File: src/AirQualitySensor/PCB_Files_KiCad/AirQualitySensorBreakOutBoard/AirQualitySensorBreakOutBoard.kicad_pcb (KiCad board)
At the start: 2 copper layers, 113.8 x 36 mm, 23 parts, among them J1 Conn_01x02_Male, J2 Conn_01x02_Male, J3 Conn_01x02_Male, J4 Conn_01x07_Male, Q1 IRLB8721PBF, U1 PMS5003, U2 PMS5003, U3 SPS30, U4 SHT31, U6 lilygo-ttgo-t-sim7000g-esp32-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

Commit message: Merged AQS
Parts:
- moved J2 0.95 mm to (93.7, 18.0)
- moved J3 0.85 mm to (93.7, 26.9)
- moved J1 0.50 mm to (93.7, 35.7)
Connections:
- U6 pad 12: unconnected-(U6-Pad12) -> VDD_EN
- U6 pad 13: VDD_EN -> unconnected-(U6-Pad13)
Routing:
- net VDD_EN: track 34.6 -> 31.9 mm
- net Solar_IN: track 41.5 -> 43.6 mm
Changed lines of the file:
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@@
   (net 7 "unconnected-(U6-Pad03)")
   (net 8 "unconnected-(U6-Pad04)")
-  (net 9 "unconnected-(U6-Pad12)")
+  (net 9 "unconnected-(U6-Pad13)")
   (net 10 "unconnected-(U6-Pad14)")
   (net 11 "unconnected-(U6-Pad15)")
@@
   (net 38 "VDD_EN")
   (footprint "Connector_JST:JST_XH_B2B-XH-AM_1x02_P2.50mm_Vertical" (layer "F.Cu")
-    (at 93.725 18.95 -90)
+    (at 93.7 18 -90)
     (descr "JST XH series connector, B2B-XH-AM, with boss (http://www.jst-mfg.com/product/pdf/eng/eXH.pdf), generated with kicad-footprint-generator")
     (tags "connector JST XH vertical boss")
@@
       (net 34 "SPI_SS") (pinfunction "SPI__SS") (pintype "input"))
     (pad "12" thru_hole circle (at -14.12 -4.6 90) (size 2 2) (drill 1.02) (layers *.Cu *.Mask)
-      (net 9 "unconnected-(U6-Pad12)") (pinfunction "12") (pintype "input"))
+      (net 38 "VDD_EN") (pinfunction "12") (pintype "input"))
     (pad "13" thru_hole circle (at -14.12 -7.14 90) (size 2 2) (drill 1.02) (layers *.Cu *.Mask)
-      (net 38 "VDD_EN") (pinfunction "13") (pintype "input"))
+      (net 9 "unconnected-(U6-Pad13)") (pinfunction "13") (pintype "input"))
     (pad "14" thru_hole circle (at -14.12 -9.68 90) (size 2 2) (drill 1.02) (layers *.Cu *.Mask)
       (net 10 "unconnected-(U6-Pad14)") (pinfunction "14") (pintype "input"))
@@
   )
   (footprint "Connector_JST:JST_XH_B2B-XH-AM_1x02_P2.50mm_Vertical" (layer "F.Cu")
-    (at 93.7 36.2 -90)
+    (at 93.7 35.7 -90)
     (descr "JST XH series connector, B2B-XH-AM, with boss (http://www.jst-mfg.com/product/pdf/eng/eXH.pdf), generated with kicad-footprint-generator")
     (tags "connector JST XH vertical boss")
@@
   )
   (footprint "Connector_JST:JST_XH_B2B-XH-AM_1x02_P2.50mm_Vertical" (layer "F.Cu")
-    (at 93.7 27.7 -90)
+    (at 93.7 26.85 -90)
     (descr "JST XH series connector, B2B-XH-AM, with boss (http://www.jst-mfg.com/product/pdf/eng/eXH.pdf), generated with kicad-footprint-generator")
     (tags "connector JST XH vertical boss")
@@
   (segment (start 57.357621 27.882379) (end 55.04 30.2) (width 1) (layer "F.Cu") (net 2))
   (segment (start 25.494649 47.243002) (end 27.537651 45.2) (width 1) (layer "F.Cu") (net 3))
+  (segment (start 93.65 29.4) (end 89.3 29.4) (width 1) (layer "F.Cu") (net 3))
   (segment (start 73.5 14.5) (end 74.9 15.9) (width 1) (layer "F.Cu") (net 3))
   (segment (start 69.4 38.4) (end 62.8 38.4) (width 1) (layer "F.Cu") (net 3))
   (segment (start 69.5 43.7) (end 70.2 43) (width 1) (layer "F.Cu") (net 3))
   (segment (start 44.9 43.7) (end 46.8 43.7) (width 1) (layer "F.Cu") (net 3))
-  (segment (start 93.7 38.7) (end 89.2 38.7) (width 1) (layer "F.Cu") (net 3))
+  (segment (start 93.7 38.35) (end 93.7 38.2) (width 1) (layer "F.Cu") (net 3))
   (segment (start 89.2 35.7) (end 89.2 29.7) (width 1) (layer "F.Cu") (net 3))
+  (segment (start 89.2 29.7) (end 89.2 20) (width 1) (layer "F.Cu") (net 3))
   (segment (start 89.2 38.7) (end 89.2 35.7) (width 1) (layer "F.Cu") (net 3))
-  (segment (start 93.7 30.2) (end 89.7 30.2) (width 1) (layer "F.Cu") (net 3))
   (segment (start 89.2 45.125) (end 89.2 38.7) (width 1) (layer "F.Cu") (net 3))
   (segment (start 46.8 43.7) (end 69.5 43.7) (width 1) (layer "F.Cu") (net 3))
+  (segment (start 89.8 20.4) (end 93.6 20.4) (width 1) (layer "F.Cu") (net 3))
   (segment (start 89.5 45.3) (end 80.2 45.3) (width 1) (layer "F.Cu") (net 3))
   (segment (start 27.537651 45.2) (end 43.4 45.2) (width 1) (layer "F.Cu") (net 3))
-  (segment (start 89.2 21.7) (end 89.45 21.45) (width 1) (layer "F.Cu") (net 3))
+  (segment (start 93.7 29.35) (end 93.65 29.4) (width 1) (layer "F.Cu") (net 3))
   (segment (start 46.617621 43.517621) (end 46.8 43.7) (width 1) (layer "F.Cu") (net 3))
   (segment (start 91.65738 45.3) (end 89.375 45.3) (width 1) (layer "F.Cu") (net 3))
@@
   (segment (start 58.394649 14.605351) (end 58.5 14.5) (width 1) (layer "F.Cu") (net 3))
   (segment (start 70.2 39.2) (end 69.4 38.4) (width 1) (layer "F.Cu") (net 3))
-  (segment (start 89.45 21.45) (end 89.95 21.45) (width 1) (layer "F.Cu") (net 3))
-  (segment (start 89.2 29.7) (end 89.2 21.7) (width 1) (layer "F.Cu") (net 3))
+  (segment (start 93.6 20.4) (end 93.7 20.5) (width 1) (layer "F.Cu") (net 3))
   (segment (start 66.8 35) (end 62 30.2) (width 1) (layer "F.Cu") (net 3))
-  (segment (start 89.95 21.45) (end 89.175 21.45) (width 1) (layer "F.Cu") (net 3))
   (segment (start 91.85738 45.2) (end 91.75738 45.3) (width 1) (layer "F.Cu") (net 3))
   (segment (start 70.2 43) (end 70.2 39.2) (width 1) (layer "F.Cu") (net 3))
   (segment (start 80.2 45.3) (end 69.9 35) (width 1) (layer "F.Cu") (net 3))
   (segment (start 69.9 35) (end 66.8 35) (width 1) (layer "F.Cu") (net 3))
-  (segment (start 89.7 30.2) (end 89.2 29.7) (width 1) (layer "F.Cu") (net 3))
   (segment (start 89.175 21.2) (end 89.175 15.9) (width 1) (layer "F.Cu") (net 3))
   (segment (start 58.394649 16.653002) (end 58.394649 14.605351) (width 1) (layer "F.Cu") (net 3))
-  (segment (start 93.792621 21.517621) (end 93.725 21.45) (width 1) (layer "F.Cu") (net 3))
   (segment (start 57.58 33.18) (end 57.58 30.2) (width 1) (layer "F.Cu") (net 3))
+  (segment (start 93.7 38.2) (end 89.3 38.2) (width 1) (layer "F.Cu") (net 3))
   (segment (start 74.9 15.9) (end 89.1 15.9) (width 1) (layer "F.Cu") (net 3))
   (segment (start 58.5 14.5) (end 73.5 14.5) (width 1) (layer "F.Cu") (net 3))
   (segment (start 91.75738 45.3) (end 91.65738 45.3) (width 1) (layer "F.Cu") (net 3))
-  (segment (start 89.95 21.45) (end 93.725 21.45) (width 1) (layer "F.Cu") (net 3))
   (segment (start 43.4 45.2) (end 44.9 43.7) (width 1) (layer "F.Cu") (net 3))
   (segment (start 30.454649 16.653002) (end 30.454649 14.5) (width 1) (layer "B.Cu") (net 3))
@@
   (segment (start 21.735 32.865) (end 19.5 35.1) (width 1) (layer "B.Cu") (net 32))
   (segment (start 22.894649 45.694649) (end 22.894649 47.263002) (width 1) (layer "B.Cu") (net 32))
-  (segment (start 97.2 28.7) (end 97.2 19.7) (width 1) (layer "F.Cu") (net 33))
-  (segment (start 97.2 27.7) (end 93.7 27.7) (width 1) (layer "F.Cu") (net 33))
+  (segment (start 97.1 26.9) (end 93.75 26.9) (width 1) (layer "F.Cu") (net 33))
+  (segment (start 97.1 35.7) (end 93.7 35.7) (width 1) (layer "F.Cu") (net 33))
+  (segment (start 97.2 18) (end 93.7 18) (width 1) (layer "F.Cu") (net 33))
+  (segment (start 97.2 35.8) (end 97.1 35.7) (width 1) (layer "F.Cu") (net 33))
+  (segment (start 97.2 28.7) (end 97.2 26.8) (width 1) (layer "F.Cu") (net 33))
   (segment (start 97.2 36.2) (end 97.2 28.7) (width 1) (layer "F.Cu") (net 33))
   (segment (start 97.2 37.7) (end 97.2 36.2) (width 1) (layer "F.Cu") (net 33))
   (segment (start 97.2 38.7) (end 97.2 37.7) (width 1) (layer "F.Cu") (net 33))
   (segment (start 97.075 45.3) (end 97.2 45.175) (width 1) (layer "F.Cu") (net 33))
-  (segment (start 96.45 18.95) (end 93.725 18.95) (width 1) (layer "F.Cu") (net 33))
-  (segment (start 97.2 36.2) (end 93.7 36.2) (width 1) (layer "F.Cu") (net 33))
-  (segment (start 97.2 19.7) (end 96.45 18.95) (width 1) (layer "F.Cu") (net 33))
-  (segment (start 97.2 28.7) (end 97.2 27.7) (width 1) (layer "F.Cu") (net 33))
+  (segment (start 97.2 28.7) (end 97.2 18) (width 1) (layer "F.Cu") (net 33))
   (segment (start 97.2 45.175) (end 97.2 37.7) (width 1) (layer "F.Cu") (net 33))
-  (segment (start 93.792621 19.017621) (end 93.725 18.95) (width 1) (layer "F.Cu") (net 33))
+  (segment (start 93.75 26.9) (end 93.7 26.85) (width 1) (layer "F.Cu") (net 33))
   (segment (start 94.15738 45.3) (end 97.075 45.3) (width 1) (layer "F.Cu") (net 33))
   (segment (start 45.694649 17.694649) (end 47.48 19.48) (width 1) (layer "F.Cu") (net 34))
@@
   (segment (start 39.86 20.5) (end 38.085 18.725) (width 1) (layer "F.Cu") (net 37))
   (segment (start 38.085 18.725) (end 38.085 16.663353) (width 1) (layer "F.Cu") (net 37))
-  (segment (start 62.5 33.51) (end 62.5 33.6) (width 1) (layer "F.Cu") (net 38))
+  (segment (start 71.6 43.8) (end 70.174649 45.225351) (width 1) (layer "F.Cu") (net 38))
+  (segment (start 62.5 33.6) (end 65.6 36.7) (width 1) (layer "F.Cu") (net 38))
   (segment (start 71.6 38.8) (end 71.6 43.8) (width 1) (layer "F.Cu") (net 38))
-  (segment (start 69.5 36.7) (end 71.6 38.8) (width 1) (layer "F.Cu") (net 38))
-  (segment (start 70.174649 45.225351) (end 55.974649 45.225351) (width 1) (layer "F.Cu") (net 38))
   (segment (start 65.6 36.7) (end 69.5 36.7) (width 1) (layer "F.Cu") (net 38))
-  (segment (start 55.974649 45.225351) (end 55.974649 47.243002) (width 1) (layer "F.Cu") (net 38))
-  (segment (start 62.5 33.6) (end 65.6 36.7) (width 1) (layer "F.Cu") (net 38))
-  (segment (start 71.6 43.8) (end 70.174649 45.225351) (width 1) (layer "F.Cu") (net 38))
+  (segment (start 62.5 33.51) (end 62.5 33.6) (width 1) (layer "F.Cu") (net 38))
+  (segment (start 69.5 36.7) (end 71.6 38.8) (width 1) (layer "F.Cu") (net 38))
+  (segment (start 58.514649 45.485351) (end 58.514649 47.243002) (width 1) (layer "F.Cu") (net 38))
+  (segment (start 58.774649 45.225351) (end 58.514649 45.485351) (width 1) (layer "F.Cu") (net 38))
+  (segment (start 70.174649 45.225351) (end 58.774649 45.225351) (width 1) (layer "F.Cu") (net 38))
 )

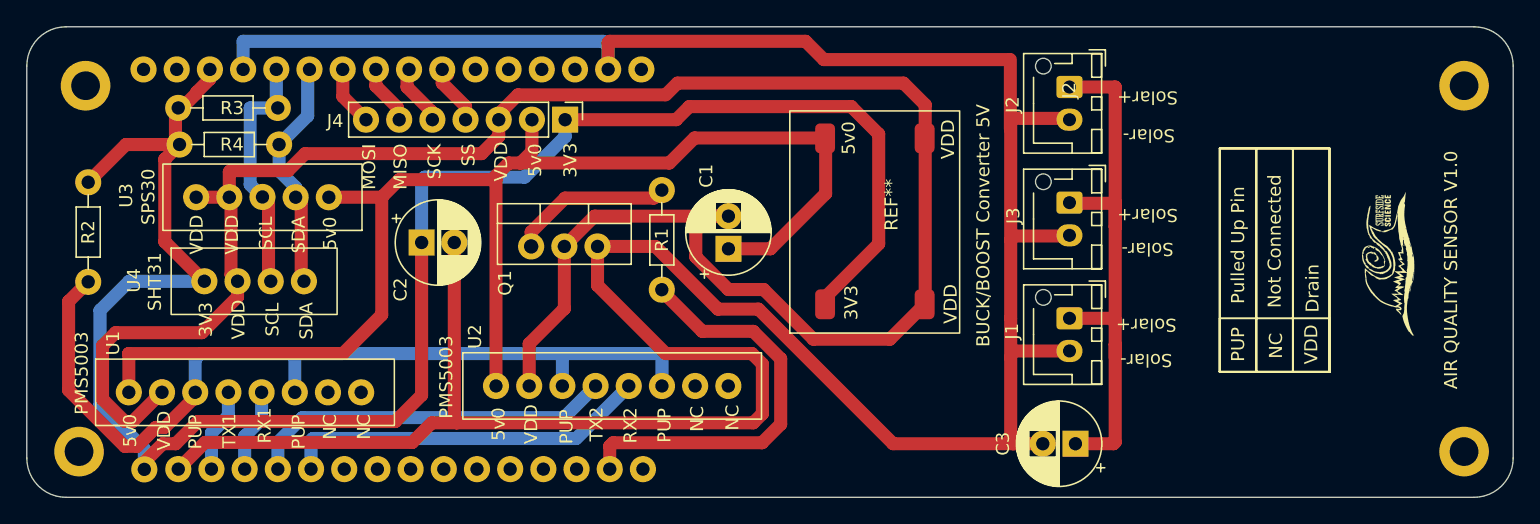
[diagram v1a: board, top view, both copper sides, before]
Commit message: Updated doc Fritzing file AQS and PCB KiCad
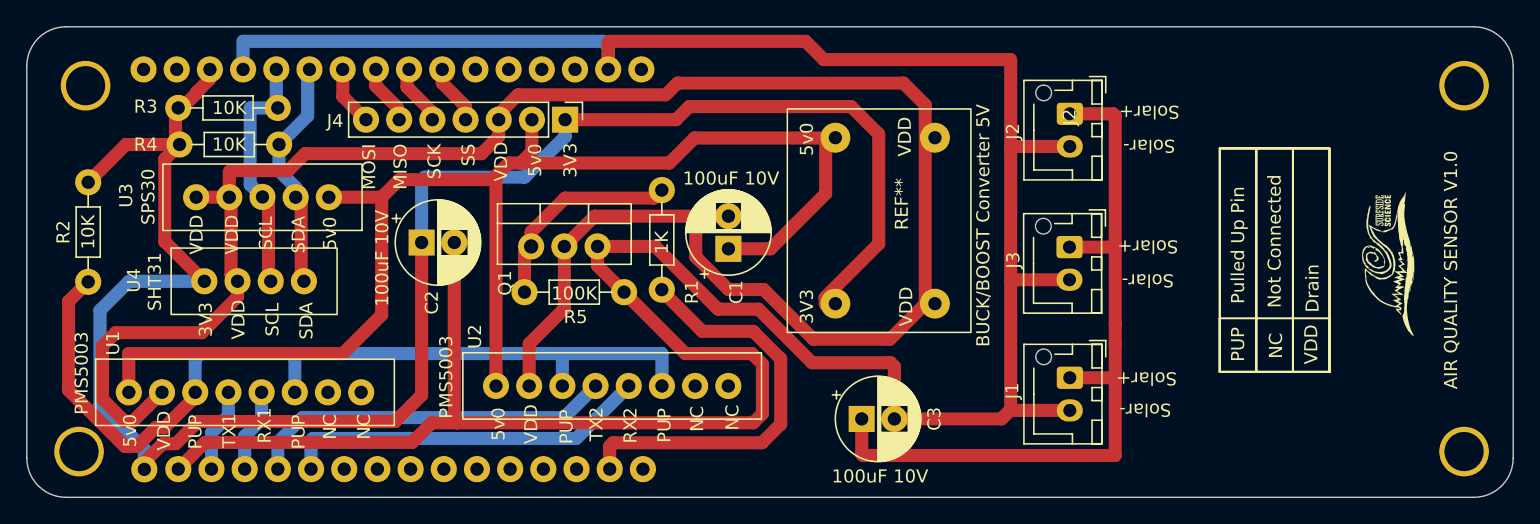
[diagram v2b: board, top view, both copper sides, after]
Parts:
- added R5: 100K, Resistor_THT:R_Axial_DIN0204_L3.6mm_D1.6mm_P7.62mm_Horizontal, F.Cu at (59.6, 33.7)
- moved C3 16.5 mm to (77.8, 43.4), turned to 0 degrees
- moved J1 4.55 mm to (93.7, 40.2)
- moved J3 3.40 mm to (93.7, 30.2)
- moved J2 2.05 mm to (93.7, 20.1)
- moved REF** 0.79 mm to (88.1, 38.7)
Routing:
- net Solar_IN: track 43.6 -> 58.9 mm
- net GND: track 231.9 -> 227.8 mm
- net Net-(Q1-Pad1): track 12.8 -> 16.5 mm
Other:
- board text added: "100K"
- board text added: "100uF 10V"
- board text added: "10K"
- board text added: "1K"
